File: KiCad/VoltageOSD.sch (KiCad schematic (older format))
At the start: 18 parts, among them J1 Camera, J2 VTX, J3 RST, J4 SCK, J5 MOSI, U1 LMH1980, U2 ATTINY13A-MMF

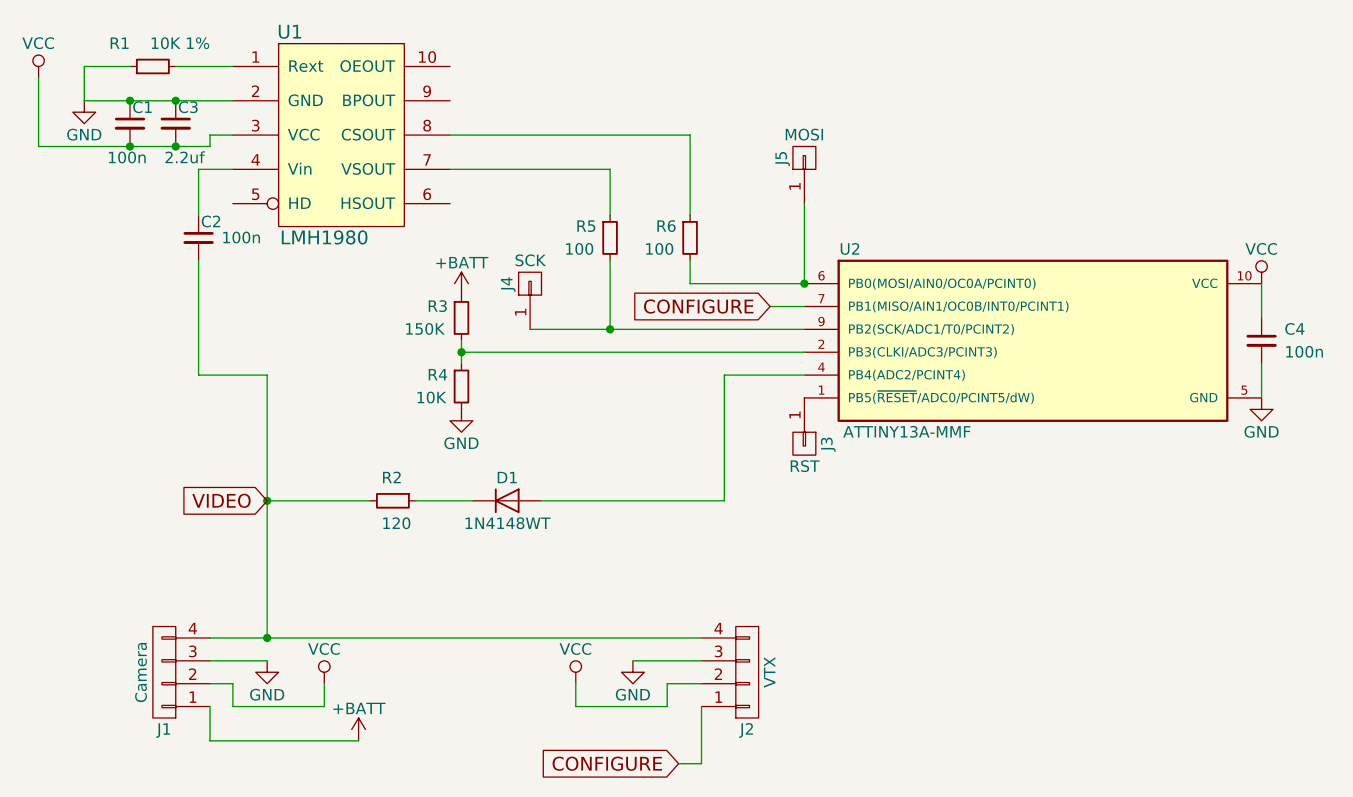
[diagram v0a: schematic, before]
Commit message: change schematic for INT0. Add ASM project.
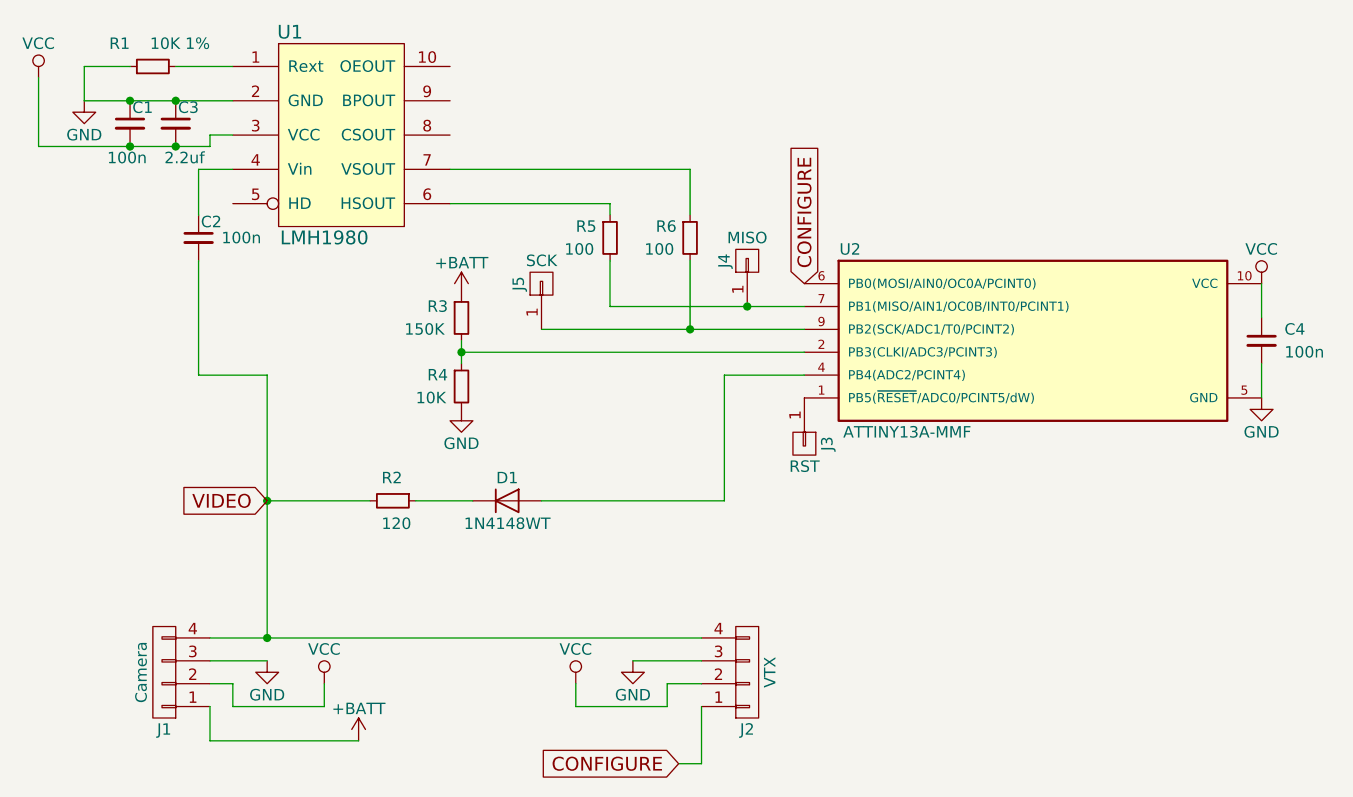
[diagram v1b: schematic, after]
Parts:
- J4: value SCK -> MISO
- J5: value MOSI -> SCK
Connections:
- net CONFIGURE: now also U2.6 (PB0(MOSI/AIN0/OC0A/PCINT0)); no longer U2.7 (PB1(MISO/AIN1/OC0B/INT0/PCINT1))
- net at J5.1 (P1), R6.2: now also U2.9 (PB2(SCK/ADC1/T0/PCINT2)); no longer U2.6 (PB0(MOSI/AIN0/OC0A/PCINT0))
- net at J4.1 (P1), R5.2: now also U2.7 (PB1(MISO/AIN1/OC0B/INT0/PCINT1)); no longer U2.9 (PB2(SCK/ADC1/T0/PCINT2))
- net at U1.6 (HSOUT): now also R5.1
- net at U1.7 (VSOUT): now also R6.1; no longer R5.1
- net at U1.8 (CSOUT): no longer R6.1
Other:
- moved on the sheet: J4, J5
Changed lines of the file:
@@
 	0    -1   -1   0
 $EndComp
-Wire Wire Line
-	2200 2500 1950 2500
 $Comp
 L GND #PWR01
@@
 	1    0    0    -1
 $EndComp
-Wire Wire Line
-	1550 2650 1750 2650
-Wire Wire Line
-	1750 2650 1950 2650
-Wire Wire Line
-	1950 2650 2200 2650
-Connection ~ 1950 2650
-Connection ~ 1750 2650
-Wire Wire Line
-	1750 2500 1550 2500
-Wire Wire Line
-	1550 2500 1550 2650
-Wire Wire Line
-	2200 2800 2100 2800
-Wire Wire Line
-	2100 2800 2100 2850
-Wire Wire Line
-	2100 2850 1950 2850
-Wire Wire Line
-	1950 2850 1750 2850
-Wire Wire Line
-	1750 2850 1350 2850
-Connection ~ 1950 2850
 $Comp
 L VCC #PWR02
@@
 	1    0    0    -1
 $EndComp
-Wire Wire Line
-	1350 2850 1350 2550
-Connection ~ 1750 2850
 $Comp
 L C_Small C2
@@
 	1    0    0    -1
 $EndComp
-Wire Wire Line
-	2200 2950 2050 2950
-Wire Wire Line
-	2050 2950 2050 3150
-Wire Wire Line
-	3150 2950 3850 2950
-Wire Wire Line
-	3500 3650 3850 3650
-Wire Wire Line
-	3850 3650 4700 3650
 $Comp
 L R_Small R5
@@
 	1    0    0    -1
 $EndComp
-Wire Wire Line
-	3850 2950 3850 3150
-Wire Wire Line
-	3850 3350 3850 3650
 $Comp
 L R_Small R6
@@
 	1    0    0    -1
 $EndComp
-Wire Wire Line
-	3150 2800 4200 2800
-Wire Wire Line
-	4200 2800 4200 3150
-Wire Wire Line
-	4700 3450 4200 3450
-Wire Wire Line
-	4200 3450 4200 3350
 $Comp
 L GND #PWR03
@@
 	0    1    1    0
 $EndComp
-Wire Wire Line
-	3250 4400 3000 4400
-Wire Wire Line
-	2050 3850 2350 3850
-Wire Wire Line
-	2350 4400 2800 4400
-Wire Wire Line
-	2050 3850 2050 3350
 $Comp
 L R_Small R3
@@
 	1    0    0    -1
 $EndComp
-Wire Wire Line
-	3200 3700 3200 3750
-Wire Wire Line
-	3200 3750 3200 3800
-Wire Wire Line
-	3200 3750 4700 3750
-Connection ~ 3200 3750
 $Comp
 L +BATT #PWR06
@@
 	1    0    0    1
 $EndComp
-Wire Wire Line
-	2100 5000 2350 5000
-Wire Wire Line
-	2350 5000 4250 5000
-Wire Wire Line
-	2350 3850 2350 4400
-Wire Wire Line
-	2350 4400 2350 5000
-Connection ~ 2350 5000
 $Comp
 L GND #PWR07
@@
 	1    0    0    -1
 $EndComp
-Wire Wire Line
-	4250 5100 3950 5100
-Wire Wire Line
-	2350 5100 2100 5100
 $Comp
 L VCC #PWR09
@@
 	1    0    0    -1
 $EndComp
-Wire Wire Line
-	2100 5200 2200 5200
-Wire Wire Line
-	2200 5200 2200 5300
-Wire Wire Line
-	2200 5300 2600 5300
-Wire Wire Line
-	2600 5300 2600 5200
-Wire Wire Line
-	3700 5200 3700 5300
-Wire Wire Line
-	3700 5300 4100 5300
-Wire Wire Line
-	4100 5300 4100 5200
-Wire Wire Line
-	4100 5200 4250 5200
 $Comp
 L +BATT #PWR011
@@
 	1    0    0    -1
 $EndComp
-Wire Wire Line
-	4150 5550 4250 5550
-Wire Wire Line
-	4250 5550 4250 5300
 Text GLabel 4150 5550 0    60   Input ~ 0
 CONFIGURE
-Wire Wire Line
-	2100 5300 2100 5450
-Wire Wire Line
-	2100 5450 2750 5450
-Text GLabel 4550 3550 0    60   Input ~ 0
+Text GLabel 4700 3450 1    60   Input ~ 0
 CONFIGURE
-Wire Wire Line
-	4700 3550 4550 3550
 Text GLabel 2350 4400 0    60   Input ~ 0
 VIDEO
@@
 	1    0    0    -1
 $EndComp
-Wire Wire Line
-	6700 3600 6700 3450
-Wire Wire Line
-	6700 3800 6700 3950
-Connection ~ 2350 4400
-Wire Wire Line
-	3550 4400 4350 4400
-Wire Wire Line
-	4350 4400 4350 3850
-Wire Wire Line
-	4350 3850 4700 3850
 $Comp
 L CONN_01X01 J3
@@
 L CONN_01X01 J5
 U 1 1 5931BD6C
-P 4700 2900
-F 0 "J5" H 4700 3000 50  0000 C CNN
-F 1 "MOSI" V 4800 2900 50  0000 C CNN
-F 2 ".pretty:Prog_pad" H 4700 2900 50  0001 C CNN
-F 3 "" H 4700 2900 50  0001 C CNN
-	1    4700 2900
+P 3550 3450
+F 0 "J5" H 3550 3550 50  0000 C CNN
+F 1 "SCK" V 3650 3450 50  0000 C CNN
+F 2 ".pretty:Prog_pad" H 3550 3450 50  0001 C CNN
+F 3 "" H 3550 3450 50  0001 C CNN
+	1    3550 3450
 	0    -1   -1   0
 $EndComp
-Wire Wire Line
-	4700 3100 4700 3450
 $Comp
 L CONN_01X01 J4
 U 1 1 5931C145
-P 3500 3450
-F 0 "J4" H 3500 3550 50  0000 C CNN
-F 1 "SCK" V 3600 3450 50  0000 C CNN
-F 2 ".pretty:Prog_pad" H 3500 3450 50  0001 C CNN
-F 3 "" H 3500 3450 50  0001 C CNN
-	1    3500 3450
+P 4450 3350
+F 0 "J4" H 4450 3450 50  0000 C CNN
+F 1 "MISO" V 4550 3350 50  0000 C CNN
+F 2 ".pretty:Prog_pad" H 4450 3350 50  0001 C CNN
+F 3 "" H 4450 3350 50  0001 C CNN
+	1    4450 3350
 	0    -1   -1   0
 $EndComp
-Connection ~ 4700 3450
-Connection ~ 3850 3650
+Wire Wire Line
+	2200 2500 1950 2500
+Wire Wire Line
+	1550 2650 2200 2650
+Connection ~ 1950 2650
+Connection ~ 1750 2650
+Wire Wire Line
+	1750 2500 1550 2500
+Wire Wire Line
+	1550 2500 1550 2650
+Wire Wire Line
+	2200 2800 2100 2800
+Wire Wire Line
+	2100 2800 2100 2850
+Wire Wire Line
+	2100 2850 1350 2850
+Connection ~ 1950 2850
+Wire Wire Line
+	1350 2850 1350 2550
+Connection ~ 1750 2850
+Wire Wire Line
+	2200 2950 2050 2950
+Wire Wire Line
+	2050 2950 2050 3150
+Wire Wire Line
+	3250 4400 3000 4400
+Wire Wire Line
+	2050 3850 2350 3850
+Wire Wire Line
+	2350 4400 2800 4400
+Wire Wire Line
+	2050 3850 2050 3350
+Wire Wire Line
+	3200 3700 3200 3800
+Wire Wire Line
+	3200 3750 4700 3750
+Connection ~ 3200 3750
+Wire Wire Line
+	2100 5000 4250 5000
+Wire Wire Line
+	2350 3850 2350 5000
+Connection ~ 2350 5000
+Wire Wire Line
+	4250 5100 3950 5100
+Wire Wire Line
+	2350 5100 2100 5100
+Wire Wire Line
+	2100 5200 2200 5200
+Wire Wire Line
+	2200 5200 2200 5300
+Wire Wire Line
+	2200 5300 2600 5300
+Wire Wire Line
+	2600 5300 2600 5200
+Wire Wire Line
+	3700 5200 3700 5300
+Wire Wire Line
+	3700 5300 4100 5300
+Wire Wire Line
+	4100 5300 4100 5200
+Wire Wire Line
+	4100 5200 4250 5200
+Wire Wire Line
+	4150 5550 4250 5550
+Wire Wire Line
+	4250 5550 4250 5300
+Wire Wire Line
+	2100 5300 2100 5450
+Wire Wire Line
+	2100 5450 2750 5450
+Wire Wire Line
+	6700 3600 6700 3450
+Wire Wire Line
+	6700 3800 6700 3950
+Connection ~ 2350 4400
+Wire Wire Line
+	3550 4400 4350 4400
+Wire Wire Line
+	4350 4400 4350 3850
+Wire Wire Line
+	4350 3850 4700 3850
+Wire Wire Line
+	3150 3100 3850 3100
+Wire Wire Line
+	3850 3100 3850 3150
+Wire Wire Line
+	3850 3350 3850 3550
+Wire Wire Line
+	3150 2950 4200 2950
+Wire Wire Line
+	4200 2950 4200 3150
+Wire Wire Line
+	3550 3650 4700 3650
+Wire Wire Line
+	4200 3350 4200 3650
+Wire Wire Line
+	3850 3550 4700 3550
+Connection ~ 4450 3550
+Connection ~ 4200 3650
 $EndSCHEMATC

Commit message: TV out partially working, but only 7 lines of char printed.
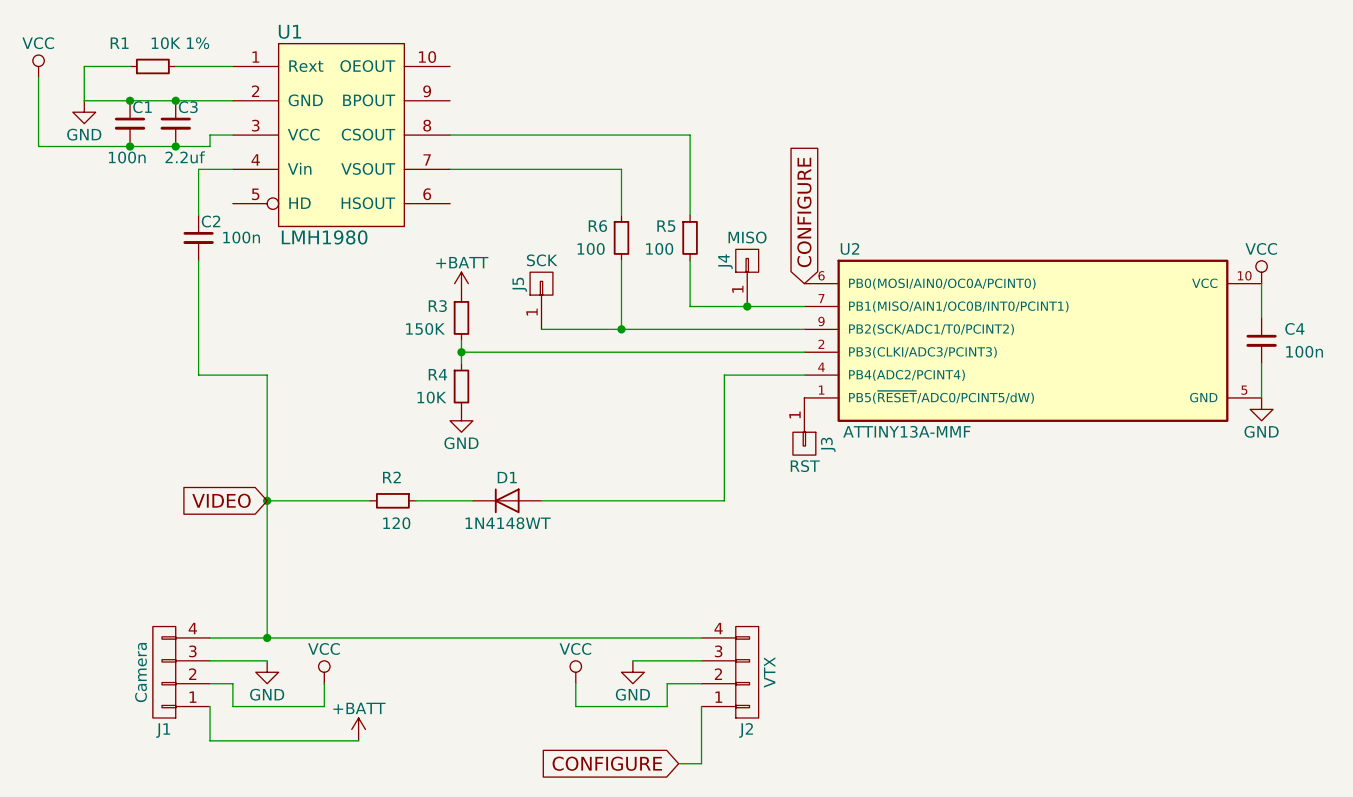
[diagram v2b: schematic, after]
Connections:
- net at U1.6 (HSOUT): no longer R5.1
- net at U1.8 (CSOUT): now also R5.1
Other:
- moved on the sheet: R5, R6
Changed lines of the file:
@@
 L R_Small R5
 U 1 1 59312BCF
-P 3850 3250
-F 0 "R5" H 3700 3300 50  0000 L CNN
-F 1 "100" H 3650 3200 50  0000 L CNN
-F 2 "Resistors_SMD:R_0402_NoSilk" H 3850 3250 50  0001 C CNN
-F 3 "" H 3850 3250 50  0001 C CNN
-	1    3850 3250
-	1    0    0    -1
-$EndComp
-$Comp
-L R_Small R6
-U 1 1 59312FDF
 P 4200 3250
-F 0 "R6" H 4050 3300 50  0000 L CNN
+F 0 "R5" H 4050 3300 50  0000 L CNN
 F 1 "100" H 4000 3200 50  0000 L CNN
 F 2 "Resistors_SMD:R_0402_NoSilk" H 4200 3250 50  0001 C CNN
 F 3 "" H 4200 3250 50  0001 C CNN
 	1    4200 3250
+	1    0    0    -1
+$EndComp
+$Comp
+L R_Small R6
+U 1 1 59312FDF
+P 3900 3250
+F 0 "R6" H 3750 3300 50  0000 L CNN
+F 1 "100" H 3700 3200 50  0000 L CNN
+F 2 "Resistors_SMD:R_0402_NoSilk" H 3900 3250 50  0001 C CNN
+F 3 "" H 3900 3250 50  0001 C CNN
+	1    3900 3250
 	1    0    0    -1
 $EndComp
@@
 	2200 2500 1950 2500
 Wire Wire Line
-	1550 2650 2200 2650
+	1550 2650 1750 2650
+Wire Wire Line
+	1750 2650 1950 2650
+Wire Wire Line
+	1950 2650 2200 2650
 Connection ~ 1950 2650
 Connection ~ 1750 2650
@@
 	2100 2800 2100 2850
 Wire Wire Line
-	2100 2850 1350 2850
+	2100 2850 1950 2850
+Wire Wire Line
+	1950 2850 1750 2850
+Wire Wire Line
+	1750 2850 1350 2850
 Connection ~ 1950 2850
 Wire Wire Line
@@
 	2050 3850 2050 3350
 Wire Wire Line
-	3200 3700 3200 3800
+	3200 3700 3200 3750
+Wire Wire Line
+	3200 3750 3200 3800
 Wire Wire Line
 	3200 3750 4700 3750
 Connection ~ 3200 3750
 Wire Wire Line
-	2100 5000 4250 5000
-Wire Wire Line
-	2350 3850 2350 5000
+	2100 5000 2350 5000
+Wire Wire Line
+	2350 5000 4250 5000
+Wire Wire Line
+	2350 3850 2350 4400
+Wire Wire Line
+	2350 4400 2350 5000
 Connection ~ 2350 5000
 Wire Wire Line
@@
 	4350 3850 4700 3850
 Wire Wire Line
-	3150 3100 3850 3100
-Wire Wire Line
-	3850 3100 3850 3150
-Wire Wire Line
-	3850 3350 3850 3550
-Wire Wire Line
-	3150 2950 4200 2950
-Wire Wire Line
-	4200 2950 4200 3150
-Wire Wire Line
-	3550 3650 4700 3650
-Wire Wire Line
-	4200 3350 4200 3650
-Wire Wire Line
-	3850 3550 4700 3550
+	4200 3350 4200 3550
+Wire Wire Line
+	3150 2950 3900 2950
+Wire Wire Line
+	3900 2950 3900 3150
+Wire Wire Line
+	3550 3650 3900 3650
+Wire Wire Line
+	3900 3650 4700 3650
+Wire Wire Line
+	3900 3350 3900 3650
+Wire Wire Line
+	4200 3550 4450 3550
+Wire Wire Line
+	4450 3550 4700 3550
 Connection ~ 4450 3550
-Connection ~ 4200 3650
+Connection ~ 3900 3650
+Wire Wire Line
+	3150 2800 4200 2800
+Wire Wire Line
+	4200 2800 4200 3150
 $EndSCHEMATC

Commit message: Final Schematic and PCB (sent to OshPark)
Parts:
- added R7: 100, Resistors_SMD:R_0402_NoSilk, symbol R_Small
- R3: value 150K -> 15K
- R4: value 10K -> 1K
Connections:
- net CONFIGURE: now also R7.1; no longer U2.6 (PB0(MOSI/AIN0/OC0A/PCINT0))
- net at U1.6 (HSOUT): now also R5.1
- net at U1.8 (CSOUT): no longer R5.1
- new net: R7.2, U2.6 (PB0(MOSI/AIN0/OC0A/PCINT0))
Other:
- moved on the sheet: J4
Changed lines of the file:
@@
 P 3200 3600
 F 0 "R3" H 3050 3650 50  0000 L CNN
-F 1 "150K" H 2950 3550 50  0000 L CNN
+F 1 "15K" H 3000 3550 50  0000 L CNN
 F 2 "Resistors_SMD:R_0402_NoSilk" H 3200 3600 50  0001 C CNN
 F 3 "" H 3200 3600 50  0001 C CNN
@@
 P 3200 3900
 F 0 "R4" H 3050 3950 50  0000 L CNN
-F 1 "10K" H 3000 3850 50  0000 L CNN
+F 1 "1K" H 3050 3850 50  0000 L CNN
 F 2 "Resistors_SMD:R_0402_NoSilk" H 3200 3900 50  0001 C CNN
 F 3 "" H 3200 3900 50  0001 C CNN
@@
 Text GLabel 4150 5550 0    60   Input ~ 0
 CONFIGURE
-Text GLabel 4700 3450 1    60   Input ~ 0
+Text GLabel 4700 3050 1    60   Input ~ 0
 CONFIGURE
 Text GLabel 2350 4400 0    60   Input ~ 0
@@
 L CONN_01X01 J4
 U 1 1 5931C145
-P 4450 3350
-F 0 "J4" H 4450 3450 50  0000 C CNN
-F 1 "MISO" V 4550 3350 50  0000 C CNN
-F 2 ".pretty:Prog_pad" H 4450 3350 50  0001 C CNN
-F 3 "" H 4450 3350 50  0001 C CNN
-	1    4450 3350
+P 4400 3350
+F 0 "J4" H 4400 3450 50  0000 C CNN
+F 1 "MISO" V 4500 3350 50  0000 C CNN
+F 2 ".pretty:Prog_pad" H 4400 3350 50  0001 C CNN
+F 3 "" H 4400 3350 50  0001 C CNN
+	1    4400 3350
 	0    -1   -1   0
 $EndComp
@@
 	2200 2500 1950 2500
 Wire Wire Line
-	1550 2650 1750 2650
-Wire Wire Line
-	1750 2650 1950 2650
-Wire Wire Line
-	1950 2650 2200 2650
+	1550 2650 2200 2650
 Connection ~ 1950 2650
 Connection ~ 1750 2650
@@
 	2100 2800 2100 2850
 Wire Wire Line
-	2100 2850 1950 2850
-Wire Wire Line
-	1950 2850 1750 2850
-Wire Wire Line
-	1750 2850 1350 2850
+	2100 2850 1350 2850
 Connection ~ 1950 2850
 Wire Wire Line
@@
 	2050 3850 2050 3350
 Wire Wire Line
-	3200 3700 3200 3750
-Wire Wire Line
-	3200 3750 3200 3800
+	3200 3700 3200 3800
 Wire Wire Line
 	3200 3750 4700 3750
 Connection ~ 3200 3750
 Wire Wire Line
-	2100 5000 2350 5000
-Wire Wire Line
-	2350 5000 4250 5000
-Wire Wire Line
-	2350 3850 2350 4400
-Wire Wire Line
-	2350 4400 2350 5000
+	2100 5000 4250 5000
+Wire Wire Line
+	2350 3850 2350 5000
 Connection ~ 2350 5000
 Wire Wire Line
@@
 	3900 2950 3900 3150
 Wire Wire Line
-	3550 3650 3900 3650
-Wire Wire Line
-	3900 3650 4700 3650
+	3550 3650 4700 3650
 Wire Wire Line
 	3900 3350 3900 3650
 Wire Wire Line
-	4200 3550 4450 3550
-Wire Wire Line
-	4450 3550 4700 3550
-Connection ~ 4450 3550
+	4200 3550 4700 3550
+Connection ~ 4400 3550
 Connection ~ 3900 3650
 Wire Wire Line
-	3150 2800 4200 2800
-Wire Wire Line
-	4200 2800 4200 3150
+	3150 3100 4200 3100
+Wire Wire Line
+	4200 3100 4200 3150
+$Comp
+L R_Small R7
+U 1 1 59390823
+P 4700 3250
+F 0 "R7" H 4550 3300 50  0000 L CNN
+F 1 "100" H 4500 3200 50  0000 L CNN
+F 2 "Resistors_SMD:R_0402_NoSilk" H 4700 3250 50  0001 C CNN
+F 3 "" H 4700 3250 50  0001 C CNN
+	1    4700 3250
+	1    0    0    -1
+$EndComp
+Wire Wire Line
+	4700 3450 4700 3350
+Wire Wire Line
+	4700 3150 4700 3050
 $EndSCHEMATC

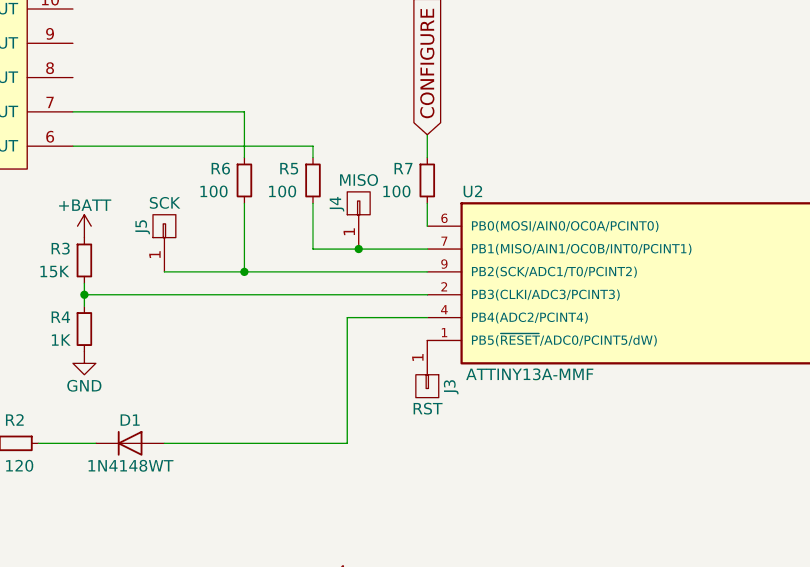
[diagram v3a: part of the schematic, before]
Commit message: Some changes to the schematic values. Added space after bitmap.
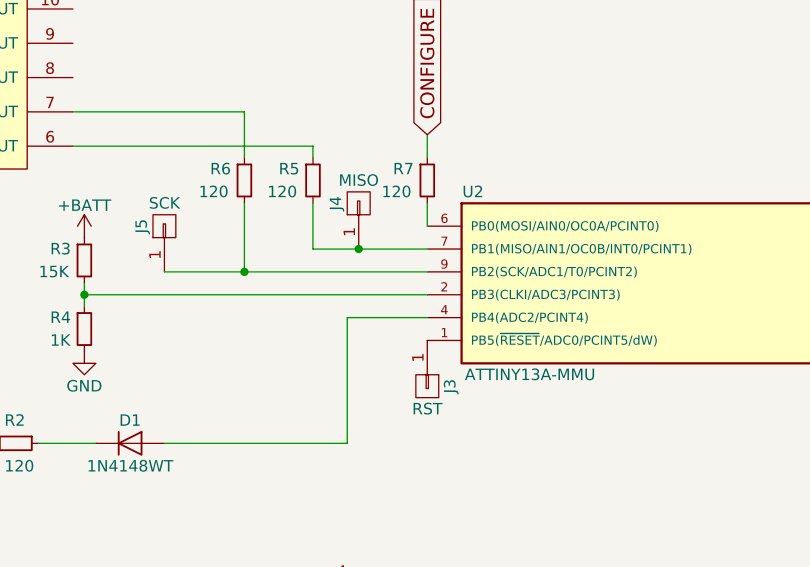
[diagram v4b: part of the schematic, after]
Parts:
- R5, R6, R7: value 100 -> 120
- U2: value ATTINY13A-MMF -> ATTINY13A-MMU
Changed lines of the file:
@@
 P 5700 3700
 F 0 "U2" H 4900 4100 50  0000 C CNN
-F 1 "ATTINY13A-MMF" H 5150 3300 50  0000 C CNN
+F 1 "ATTINY13A-MMU" H 5150 3300 50  0000 C CNN
 F 2 ".pretty:MLF_10M1" H 6300 3700 50  0001 C CIN
 F 3 "" H 4900 4050 50  0001 C CNN
@@
 P 4200 3250
 F 0 "R5" H 4050 3300 50  0000 L CNN
-F 1 "100" H 4000 3200 50  0000 L CNN
+F 1 "120" H 4000 3200 50  0000 L CNN
 F 2 "Resistors_SMD:R_0402_NoSilk" H 4200 3250 50  0001 C CNN
 F 3 "" H 4200 3250 50  0001 C CNN
@@
 P 3900 3250
 F 0 "R6" H 3750 3300 50  0000 L CNN
-F 1 "100" H 3700 3200 50  0000 L CNN
+F 1 "120" H 3700 3200 50  0000 L CNN
 F 2 "Resistors_SMD:R_0402_NoSilk" H 3900 3250 50  0001 C CNN
 F 3 "" H 3900 3250 50  0001 C CNN
@@
 P 4700 3250
 F 0 "R7" H 4550 3300 50  0000 L CNN
-F 1 "100" H 4500 3200 50  0000 L CNN
+F 1 "120" H 4500 3200 50  0000 L CNN
 F 2 "Resistors_SMD:R_0402_NoSilk" H 4700 3250 50  0001 C CNN
 F 3 "" H 4700 3250 50  0001 C CNN
